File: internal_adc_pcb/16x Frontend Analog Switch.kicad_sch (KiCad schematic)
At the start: 25 parts, among them U1 RS2323XUTQK10, U2 RS2323XUTQK10, U3 RS2323XUTQK10, U4 RS2323XUTQK10, U5 RS2323XUTQK10, U6 RS2323XUTQK10, U7 RS2323XUTQK10, U8 RS2323XUTQK10

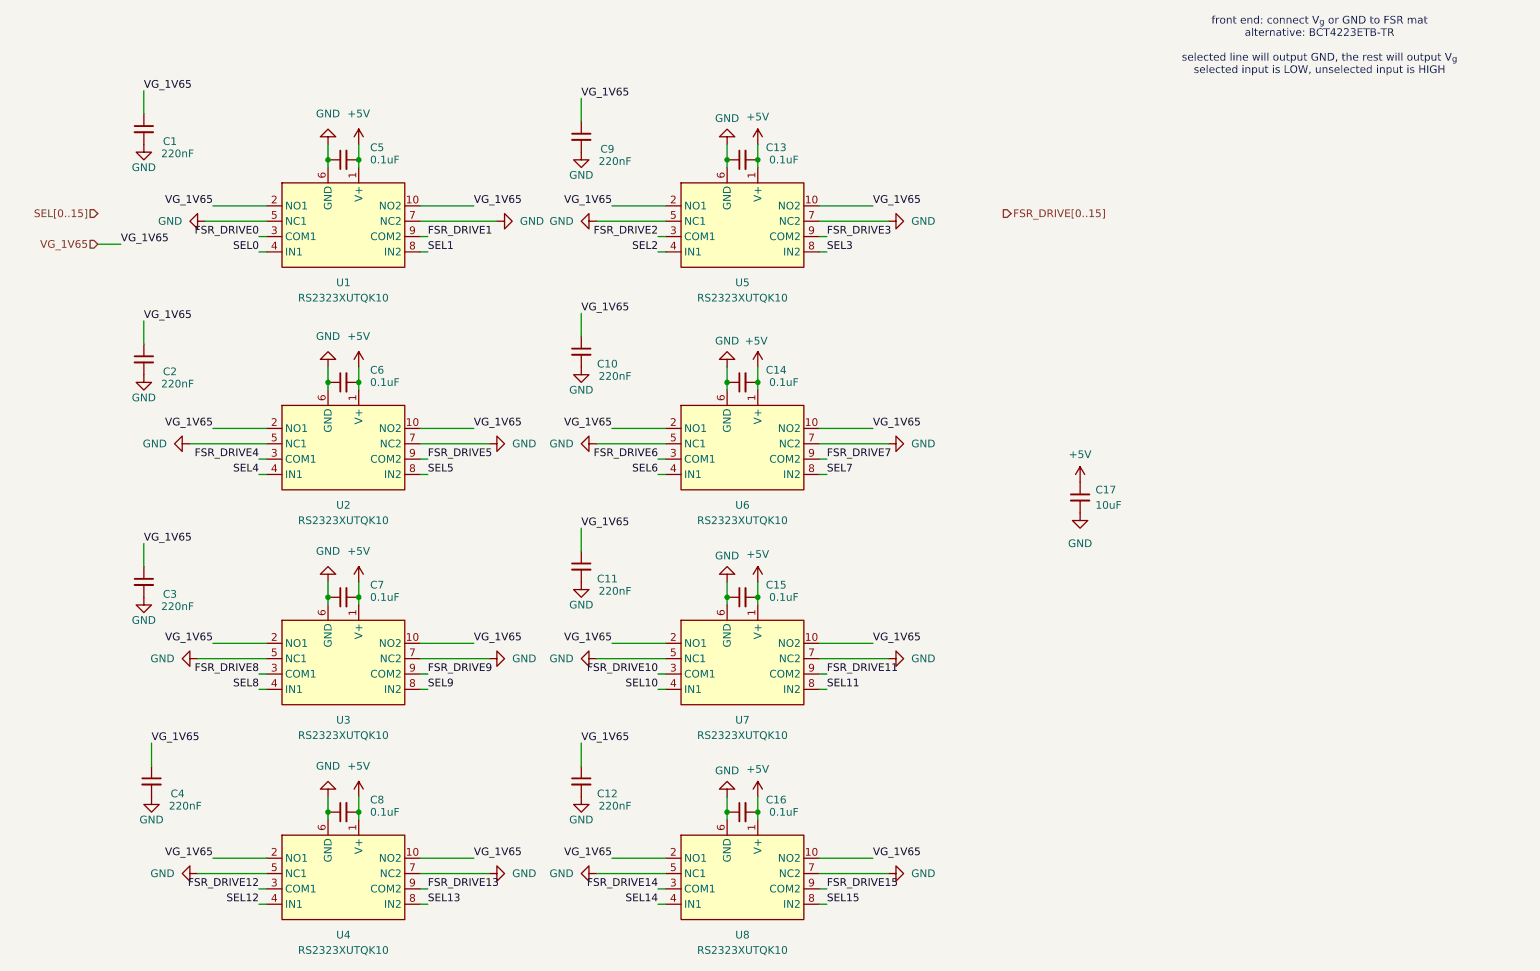
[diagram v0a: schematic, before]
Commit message: adjust VG issue for internal ADC version; changed naming for VG
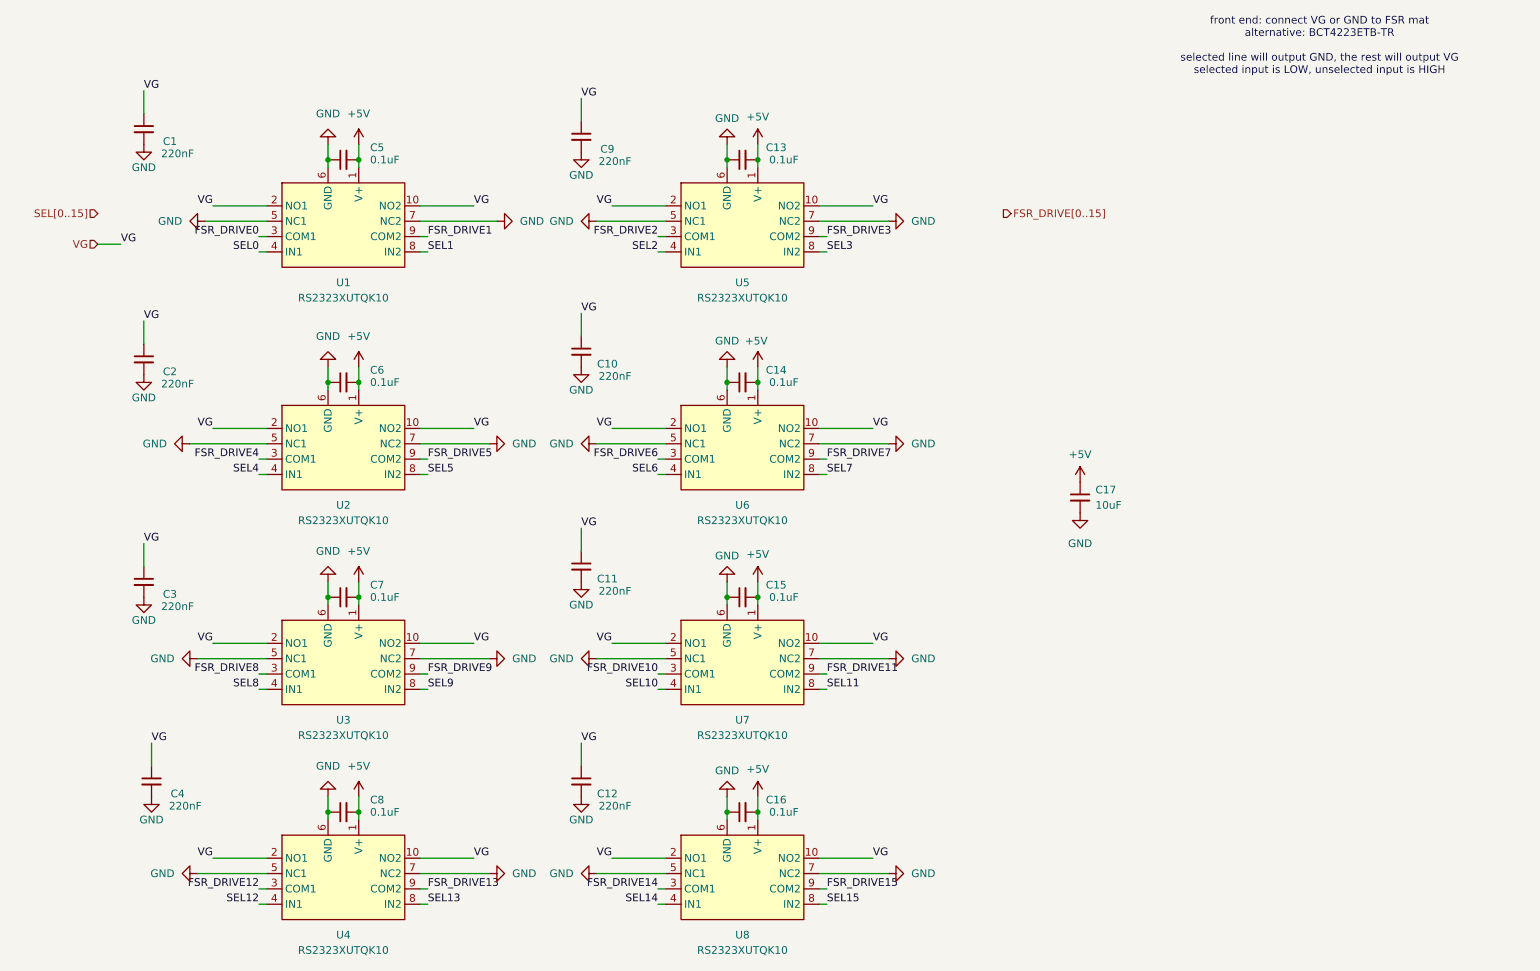
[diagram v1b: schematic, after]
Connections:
- net VG_1V65 renamed VG
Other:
- note added: "front end: connect VG or GND to FSR mat alternative: BCT4223ETB-TR selected line will output GND, the rest will output VG selected input is LOW, unselected input is HIGH"
- note removed: "front end: connect V_{g} or GND to FSR mat alternative: BCT4223ETB-TR selected line will output GND, the rest will output V_{g} selected input is LOW, unselected input is HIGH"
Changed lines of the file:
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@@
 	(generator_version "10.0")
 	(paper "A4")
-	(text "front end: connect V_{g} or GND to FSR mat\nalternative: BCT4223ETB-TR\n\nselected line will output GND, the rest will output V_{g} \nselected input is LOW, unselected input is HIGH"
+	(text "front end: connect VG or GND to FSR mat\nalternative: BCT4223ETB-TR\n\nselected line will output GND, the rest will output VG \nselected input is LOW, unselected input is HIGH"
 		(exclude_from_sim no)
 		(at 239.014 23.114 0)
@@
 		)
 	)
-	(label "VG_1V65"
+	(label "VG"
 		(at 116.84 102.87 0)
 		(effects
@@
 		)
 	)
-	(label "VG_1V65"
+	(label "VG"
 		(at 99.06 157.48 0)
 		(effects
@@
 		)
 	)
-	(label "VG_1V65"
+	(label "VG"
 		(at 121.92 49.53 180)
 		(effects
@@
 		)
 	)
-	(label "VG_1V65"
+	(label "VG"
 		(at 165.1 121.92 0)
 		(effects
@@
 		)
 	)
-	(label "VG_1V65"
+	(label "VG"
 		(at 44.45 30.48 0)
 		(effects
@@
 		)
 	)
-	(label "VG_1V65"
+	(label "VG"
 		(at 116.84 138.43 0)
 		(effects
@@
 		)
 	)
-	(label "VG_1V65"
+	(label "VG"
 		(at 121.92 86.36 180)
 		(effects
@@
 		)
 	)
-	(label "VG_1V65"
+	(label "VG"
 		(at 40.64 55.88 0)
 		(effects
@@
 		)
 	)
-	(label "VG_1V65"
+	(label "VG"
 		(at 99.06 121.92 0)
 		(effects
@@
 		)
 	)
-	(label "VG_1V65"
+	(label "VG"
 		(at 116.84 67.31 0)
 		(effects
@@
 		)
 	)
-	(label "VG_1V65"
+	(label "VG"
 		(at 99.06 86.36 0)
 		(effects
@@
 		)
 	)
-	(label "VG_1V65"
+	(label "VG"
 		(at 165.1 157.48 0)
 		(effects
@@
 		)
 	)
-	(label "VG_1V65"
+	(label "VG"
 		(at 55.88 157.48 180)
 		(effects
@@
 		)
 	)
-	(label "VG_1V65"
+	(label "VG"
 		(at 165.1 86.36 0)
 		(effects
@@
 		)
 	)
-	(label "VG_1V65"
+	(label "VG"
 		(at 121.92 157.48 180)
 		(effects
@@
 		)
 	)
-	(label "VG_1V65"
+	(label "VG"
 		(at 165.1 49.53 0)
 		(effects
@@
 		)
 	)
-	(label "VG_1V65"
+	(label "VG"
 		(at 99.06 49.53 0)
 		(effects
@@
 		)
 	)
-	(label "VG_1V65"
+	(label "VG"
 		(at 44.45 105.41 0)
 		(effects
@@
 		)
 	)
-	(label "VG_1V65"
+	(label "VG"
 		(at 55.88 49.53 180)
 		(effects
@@
 		)
 	)
-	(label "VG_1V65"
+	(label "VG"
 		(at 116.84 31.75 0)
 		(effects
@@
 		)
 	)
-	(label "VG_1V65"
+	(label "VG"
 		(at 44.45 68.58 0)
 		(effects
@@
 		)
 	)
-	(label "VG_1V65"
+	(label "VG"
 		(at 45.72 138.43 0)
 		(effects
@@
 		)
 	)
-	(label "VG_1V65"
+	(label "VG"
 		(at 55.88 121.92 180)
 		(effects
@@
 		)
 	)
-	(label "VG_1V65"
+	(label "VG"
 		(at 55.88 86.36 180)
 		(effects
@@
 		)
 	)
-	(label "VG_1V65"
+	(label "VG"
 		(at 121.92 121.92 180)
 		(effects
@@
 		)
 	)
-	(hierarchical_label "VG_1V65"
+	(hierarchical_label "VG"
 		(shape input)
 		(at 36.83 55.88 180)

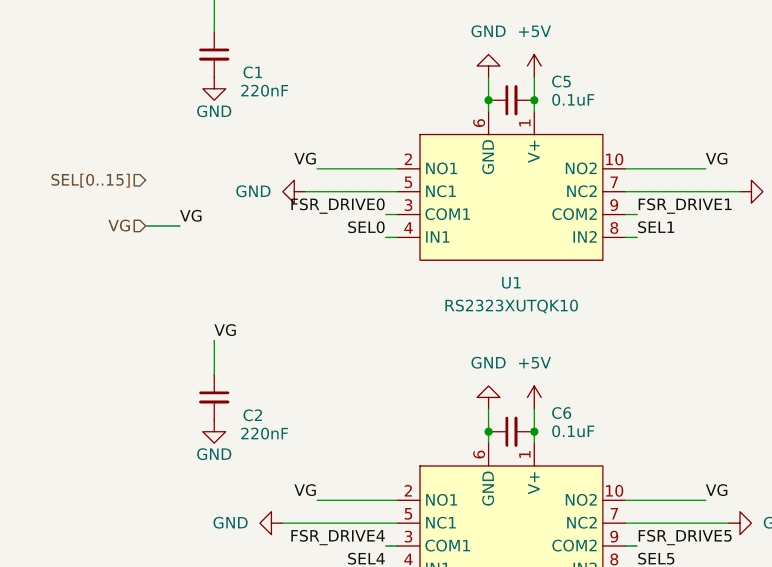
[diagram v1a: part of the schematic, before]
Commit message: update pcb for internal adc version
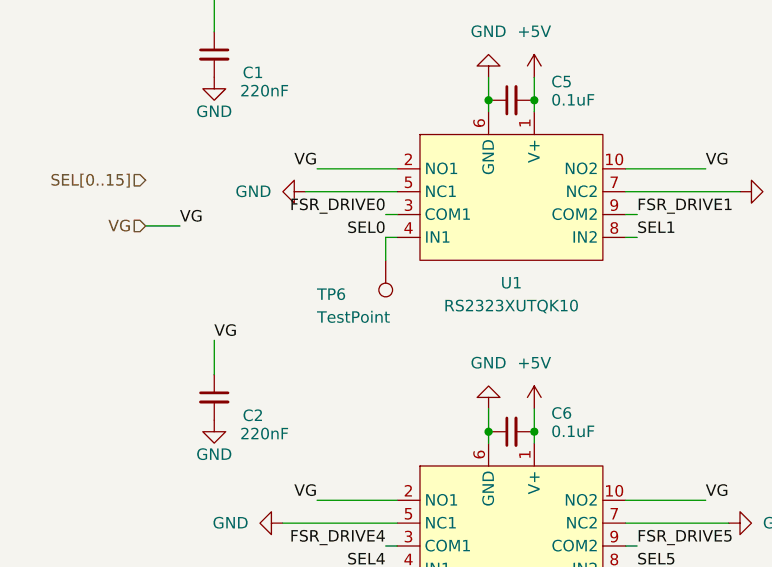
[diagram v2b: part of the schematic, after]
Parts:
- added TP6: TestPoint, TestPoint:TestPoint_Keystone_5000-5004_Miniature, symbol Connector:TestPoint
- C1, C10, C11, C12, C13, C14, C15, C16, C17, C2, C3, C4, C5, C6, C7, C8, C9: footprint (none) -> Capacitor_SMD:C_0603_1608Metric
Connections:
- net SEL0: now also TP6.1
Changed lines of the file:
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@@
 	(wire
 		(pts
+			(xy 63.5 57.15) (xy 64.77 57.15)
+		)
+		(stroke
+			(width 0)
+			(type default)
+		)
+	)
+	(wire
+		(pts
 			(xy 121.92 121.92) (xy 130.81 121.92)
 		)
@@
 	(wire
 		(pts
-			(xy 63.5 57.15) (xy 64.77 57.15)
-		)
-		(stroke
-			(width 0)
-			(type default)
-		)
-	)
-	(wire
-		(pts
 			(xy 157.48 129.54) (xy 156.21 129.54)
 		)
@@
 	(wire
 		(pts
+			(xy 63.5 57.15) (xy 63.5 59.69)
+		)
+		(stroke
+			(width 0)
+			(type default)
+		)
+	)
+	(wire
+		(pts
 			(xy 129.54 93.98) (xy 130.81 93.98)
 		)
@@
 			)
 		)
-		(property "Footprint" ""
+		(property "Footprint" "Capacitor_SMD:C_0603_1608Metric"
 			(at 116.84 144.78 0)
 			(hide yes)
@@
 			)
 		)
-		(property "Footprint" ""
+		(property "Footprint" "Capacitor_SMD:C_0603_1608Metric"
 			(at 77.47 78.74 0)
 			(hide yes)
@@
 			)
 		)
-		(property "Footprint" ""
+		(property "Footprint" "Capacitor_SMD:C_0603_1608Metric"
 			(at 143.51 41.91 0)
 			(hide yes)
@@
 			)
 		)
-		(property "Footprint" ""
+		(property "Footprint" "Capacitor_SMD:C_0603_1608Metric"
 			(at 143.51 149.86 0)
 			(hide yes)
@@
 			)
 		)
-		(property "Footprint" ""
+		(property "Footprint" "Capacitor_SMD:C_0603_1608Metric"
 			(at 77.47 114.3 0)
 			(hide yes)
@@
 			)
 		)
-		(property "Footprint" ""
+		(property "Footprint" "Capacitor_SMD:C_0603_1608Metric"
 			(at 116.84 73.66 0)
 			(hide yes)
@@
 			)
 		)
-		(property "Footprint" ""
+		(property "Footprint" "Capacitor_SMD:C_0603_1608Metric"
 			(at 199.39 97.79 0)
 			(hide yes)
@@
 			)
 		)
-		(property "Footprint" ""
+		(property "Footprint" "Capacitor_SMD:C_0603_1608Metric"
 			(at 143.51 114.3 0)
 			(hide yes)
@@
 			)
 		)
-		(property "Footprint" ""
+		(property "Footprint" "Capacitor_SMD:C_0603_1608Metric"
 			(at 116.84 109.22 0)
 			(hide yes)
@@
 			)
 		)
-		(property "Footprint" ""
+		(property "Footprint" "Capacitor_SMD:C_0603_1608Metric"
 			(at 44.45 74.93 0)
 			(hide yes)
@@
 			)
 		)
-		(property "Footprint" ""
+		(property "Footprint" "Capacitor_SMD:C_0603_1608Metric"
 			(at 44.45 111.76 0)
 			(hide yes)
@@
 			)
 		)
-		(property "Footprint" ""
+		(property "Footprint" "Capacitor_SMD:C_0603_1608Metric"
 			(at 143.51 78.74 0)
 			(hide yes)
@@
 			)
 		)
-		(property "Footprint" ""
+		(property "Footprint" "Capacitor_SMD:C_0603_1608Metric"
 			(at 44.45 36.83 0)
 			(hide yes)
@@
 			)
 		)
-		(property "Footprint" ""
+		(property "Footprint" "Capacitor_SMD:C_0603_1608Metric"
 			(at 116.84 38.1 0)
 			(hide yes)
@@
 			)
 		)
-		(property "Footprint" ""
+		(property "Footprint" "Capacitor_SMD:C_0603_1608Metric"
 			(at 45.72 144.78 0)
 			(hide yes)
@@
 	)
 	(symbol
+		(lib_id "Connector:TestPoint")
+		(at 63.5 59.69 180)
+		(unit 1)
+		(body_style 1)
+		(exclude_from_sim no)
+		(in_bom yes)
+		(on_board yes)
+		(in_pos_files yes)
+		(dnp no)
+		(property "Reference" "TP6"
+			(at 55.88 63.5 0)
+			(show_name no)
+			(do_not_autoplace no)
+			(effects
+				(font
+					(size 1.27 1.27)
+				)
+				(justify right)
+			)
+		)
+		(property "Value" "TestPoint"
+			(at 55.88 66.04 0)
+			(show_name no)
+			(do_not_autoplace no)
+			(effects
+				(font
+					(size 1.27 1.27)
+				)
+				(justify right)
+			)
+		)
+		(property "Footprint" "TestPoint:TestPoint_Keystone_5000-5004_Miniature"
+			(at 58.42 59.69 0)
+			(hide yes)
+			(show_name no)
+			(do_not_autoplace no)
+			(effects
+				(font
+					(size 1.27 1.27)
+				)
+			)
+		)
+		(property "Datasheet" ""
+			(at 58.42 59.69 0)
+			(hide yes)
+			(show_name no)
+			(do_not_autoplace no)
+			(effects
+				(font
+					(size 1.27 1.27)
+				)
+			)
+		)
+		(property "Description" "test point"
+			(at 63.5 59.69 0)
+			(hide yes)
+			(show_name no)
+			(do_not_autoplace no)
+			(effects
+				(font
+					(size 1.27 1.27)
+				)
+			)
+		)
+		(pin "1"
+		)
+		(instances
+			(project "fsr_matrix_readout_internal_adc"
+				(path "/a2a8c34e-3adf-4a95-8857-b713f7048029/307fdc1f-8268-4192-8310-111e61425162"
+					(reference "TP6")
+					(unit 1)
+				)
+			)
+		)
+	)
+	(symbol
 		(lib_id "power:+5V")
 		(at 80.01 39.37 0)
@@
 			)
 		)
-		(property "Footprint" ""
+		(property "Footprint" "Capacitor_SMD:C_0603_1608Metric"
 			(at 77.47 149.86 0)
 			(hide yes)
@@
 			)
 		)
-		(property "Footprint" ""
+		(property "Footprint" "Capacitor_SMD:C_0603_1608Metric"
 			(at 77.47 41.91 0)
 			(hide yes)
